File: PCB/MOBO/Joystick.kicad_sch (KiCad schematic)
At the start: 23 parts, among them J107 DTR, J107 MISO, J107 MOSI, J107 RXD, J107 SCK, J107 TXD, SW301 RS Button, SW302 LS Button, SW303 DPAD Right, SW304 DPAD Left, SW305 Reset_Button, SW306 B Button, SW307 A Button, SW308 DPAD Down, SW309 DPAD Up, U301 ATmega328PB-M, Y301 YABM11-16.000MHZ-12-B1U-T

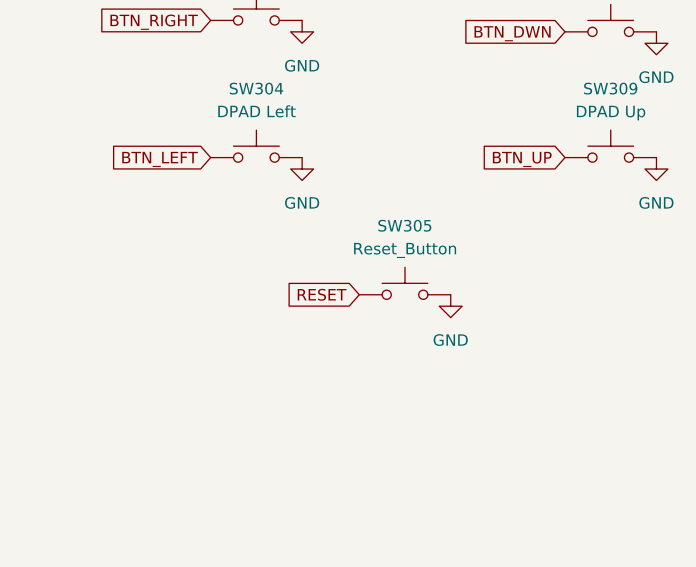
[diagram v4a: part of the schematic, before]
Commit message: switched to a pad for atmega reset
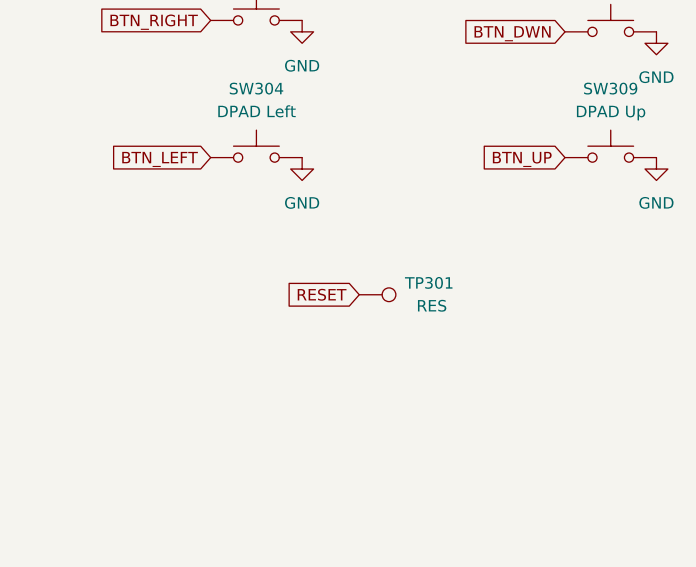
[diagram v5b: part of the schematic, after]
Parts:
- removed SW305: Reset_Button, Button_Switch_SMD:SW_SPST_Omron_B3FS-100xP, symbol Switch:SW_Omron_B3FS
- added TP301: RES, TestPoint:TestPoint_Pad_D1.0mm, symbol Connector:TestPoint
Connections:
- net RESET: now also TP301.1
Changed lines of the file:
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@@
-    )
-  )
-  (symbol (lib_id "power:GND") (at 220.98 82.55 0) (unit 1)
-    (in_bom yes) (on_board yes) (dnp no) (fields_autoplaced)
-    (property "Reference" "#PWR0307" (at 220.98 88.9 0)
-      (effects (font (size 1.27 1.27)) hide)
-    )
-    (property "Value" "GND" (at 220.98 87.63 0)
-      (effects (font (size 1.27 1.27)))
-    )
-    (property "Footprint" "" (at 220.98 82.55 0)
-      (effects (font (size 1.27 1.27)) hide)
-    )
-    (property "Datasheet" "" (at 220.98 82.55 0)
-      (effects (font (size 1.27 1.27)) hide)
-    )
-    (pin "1")
-    (instances
-      (project "MOBO"
-        (path "/2d62a3c1-c4f2-4921-9f6b-8dc8aef69d64/7ca0e1b4-2467-452a-8d82-c598e33fab6f"
-          (reference "#PWR0307") (unit 1)
-        )
-      )
     )
   )
@@
     )
   )
-  (symbol (lib_id "Switch:SW_Omron_B3FS") (at 215.9 82.55 0) (unit 1)
-    (in_bom yes) (on_board yes) (dnp no) (fields_autoplaced)
-    (property "Reference" "SW305" (at 215.9 74.93 0)
-      (effects (font (size 1.27 1.27)))
-    )
-    (property "Value" "Reset_Button" (at 215.9 77.47 0)
-      (effects (font (size 1.27 1.27)))
-    )
-    (property "Footprint" "Button_Switch_SMD:SW_SPST_Omron_B3FS-100xP" (at 215.9 77.47 0)
-      (effects (font (size 1.27 1.27)) hide)
-    )
-    (property "Datasheet" "https://octopart.com/b3f-4000-omron-22510?r=sp" (at 215.9 77.47 0)
-      (effects (font (size 1.27 1.27)) hide)
-    )
-    (pin "2")
-    (pin "1")
-    (instances
-      (project "MOBO"
-        (path "/2d62a3c1-c4f2-4921-9f6b-8dc8aef69d64/7ca0e1b4-2467-452a-8d82-c598e33fab6f"
-          (reference "SW305") (unit 1)
-        )
-      )
-    )
-  )
   (symbol (lib_id "Switch:SW_Omron_B3FS") (at 199.39 67.31 0) (unit 1)
     (in_bom yes) (on_board yes) (dnp no) (fields_autoplaced)
@@
         )
       )
+    )
+  )
+  (symbol (lib_id "Connector:TestPoint") (at 210.82 82.55 270) (unit 1)
+    (in_bom yes) (on_board yes) (dnp no)
+    (property "Reference" "TP301" (at 215.9 81.28 90)
+      (effects (font (size 1.27 1.27)) (justify left))
+    )
+    (property "Value" "RES" (at 217.17 83.82 90)
+      (effects (font (size 1.27 1.27)) (justify left))
+    )
+    (property "Footprint" "TestPoint:TestPoint_Pad_D1.0mm" (at 210.82 87.63 0)
+      (effects (font (size 1.27 1.27)) hide)
+    )
+    (property "Datasheet" "~" (at 210.82 87.63 0)
+      (effects (font (size 1.27 1.27)) hide)
+    )
+    (pin "1")
+    (instances
+      (project "MOBO"
+        (path "/2d62a3c1-c4f2-4921-9f6b-8dc8aef69d64/7ca0e1b4-2467-452a-8d82-c598e33fab6f"
+          (reference "TP301") (unit 1)
+        )
+      )

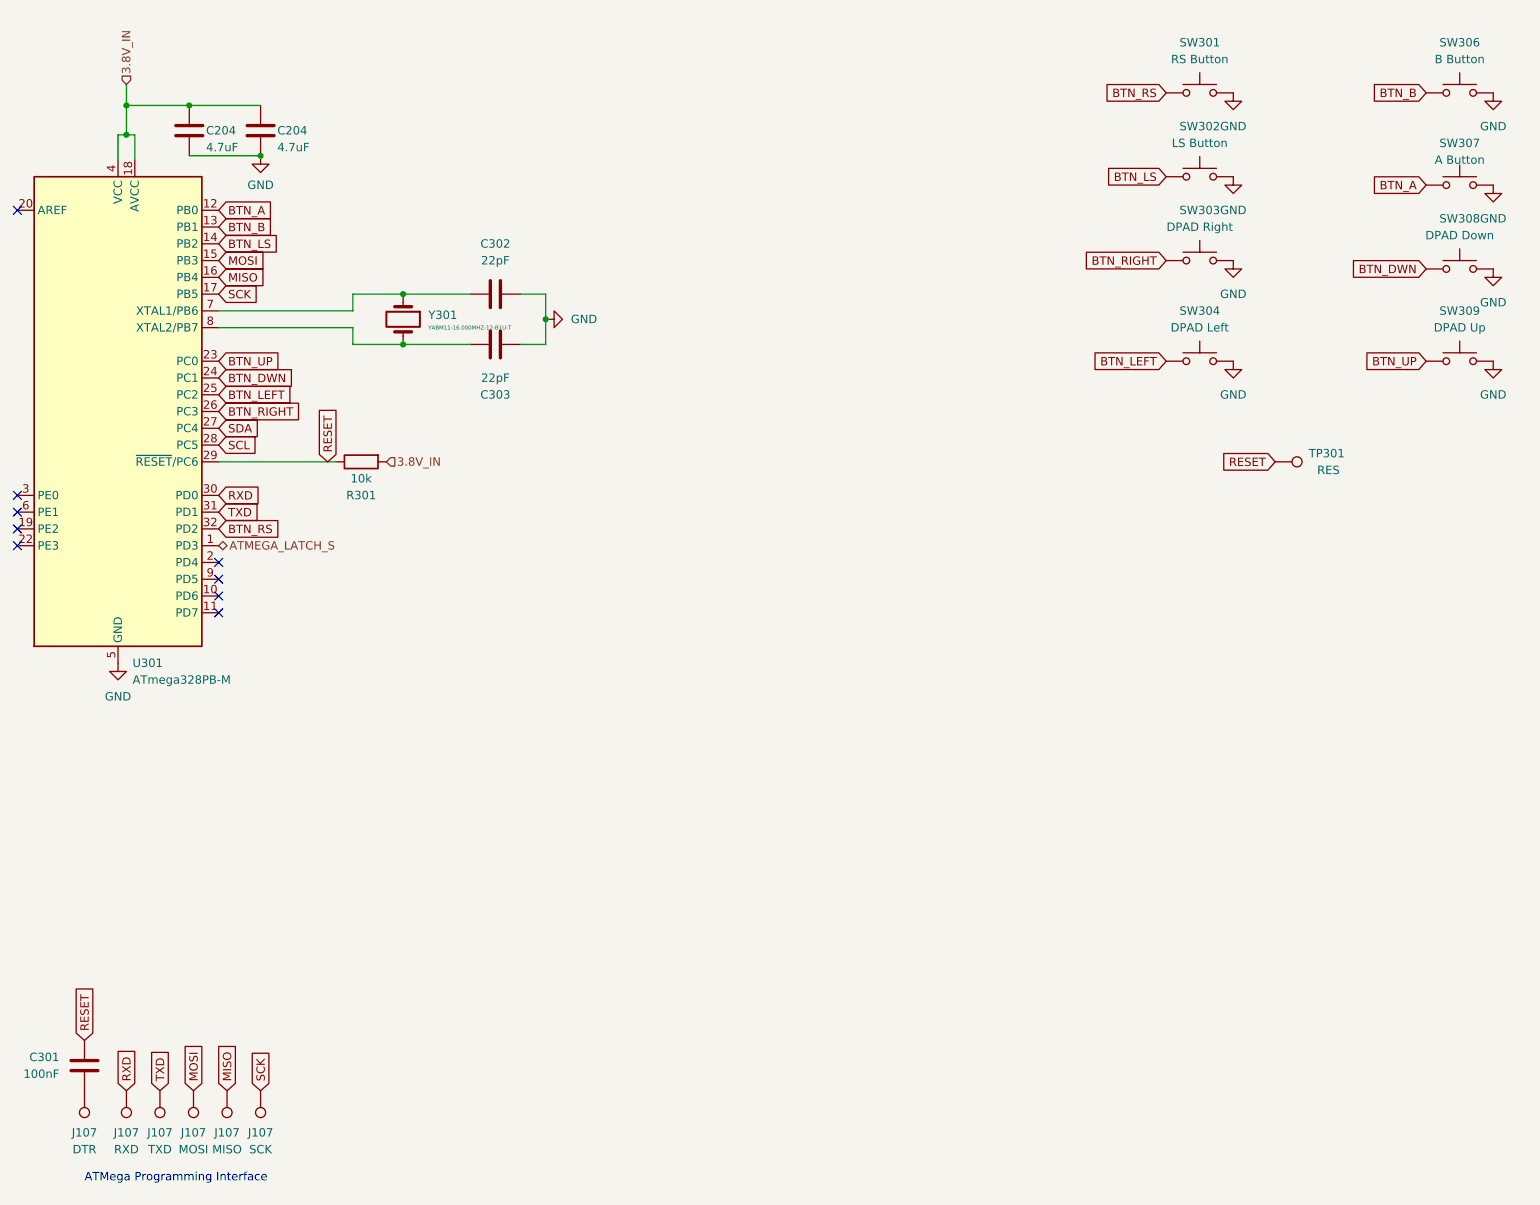
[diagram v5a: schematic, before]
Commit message: fixed schematic net names
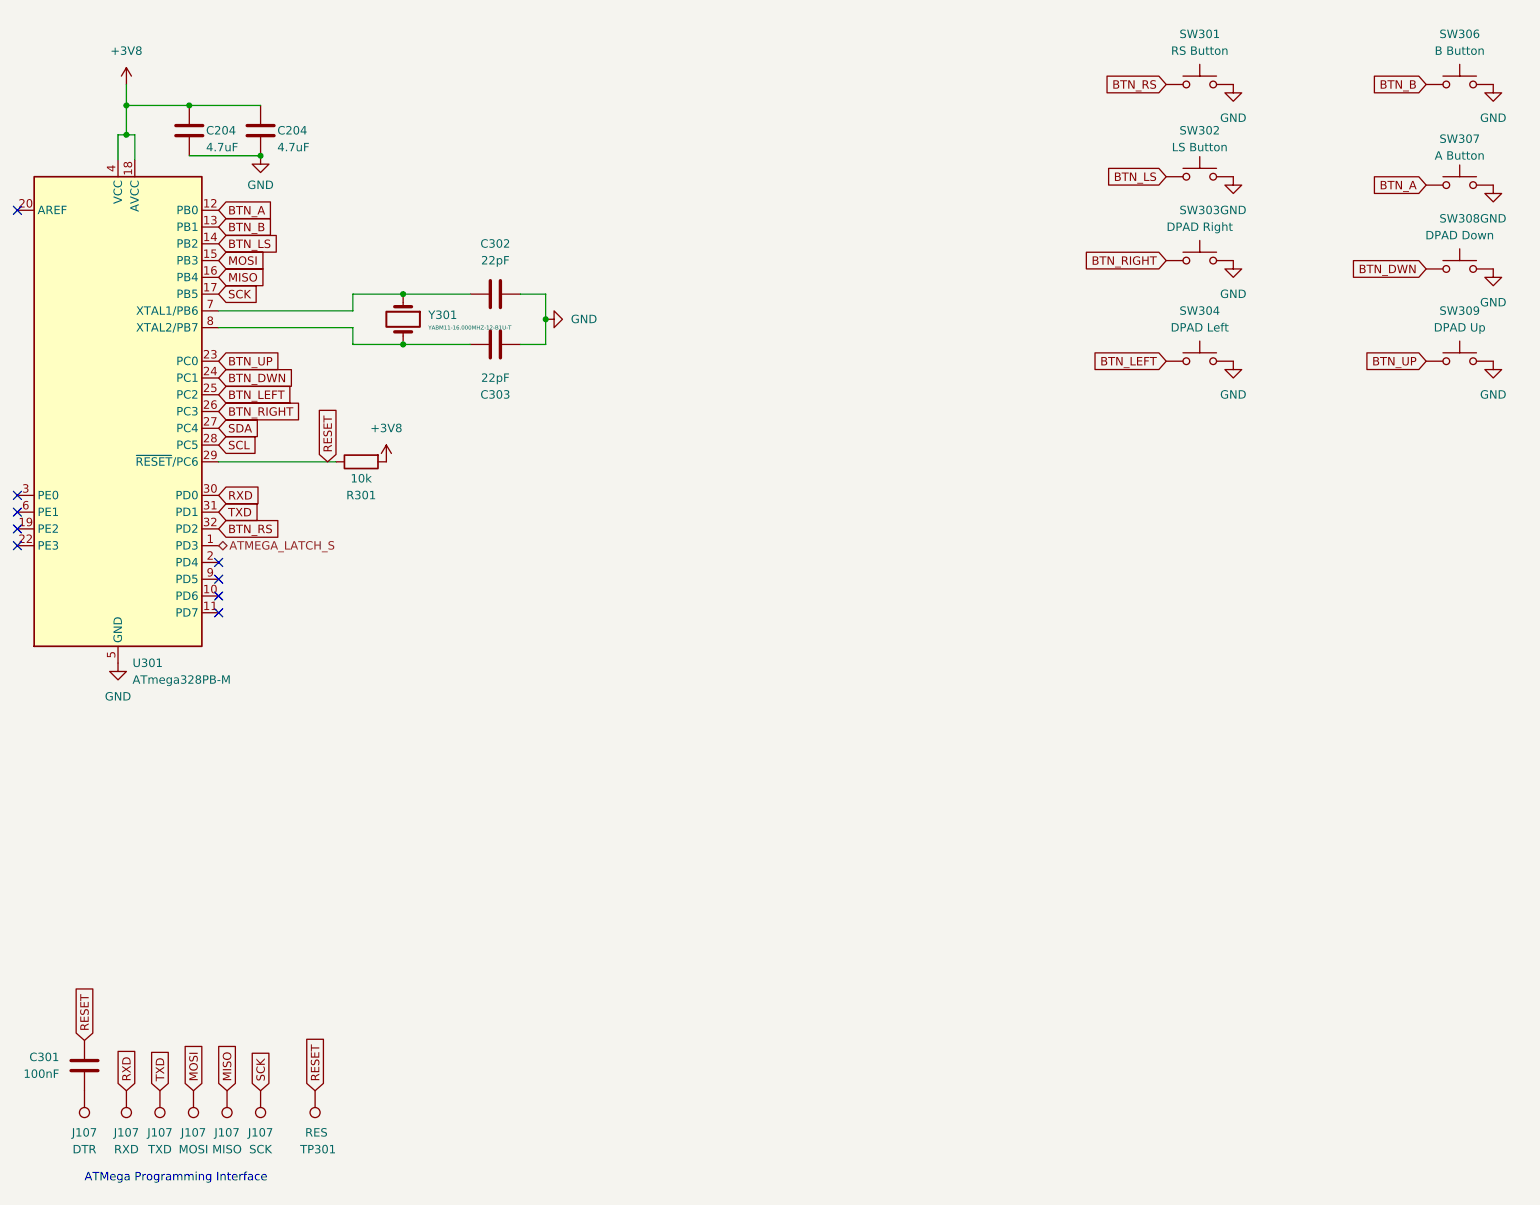
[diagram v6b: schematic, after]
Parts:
- SW301, SW302: footprint Button_Switch_SMD:SW_SPST_Omron_B3FS-100xP -> Button_Switch_THT:SW_SPST_Omron_B3F-315x_Angled
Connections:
- net 3.8V_IN renamed +3V8
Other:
- moved on the sheet: SW301, SW306, TP301
